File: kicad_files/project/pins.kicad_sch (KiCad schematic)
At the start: 0 parts

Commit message: started with board layout, also added more stuff on the schematic
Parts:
- added J3: Conn_02x11_Odd_Even, Connector_PinHeader_2.54mm:PinHeader_2x11_P2.54mm_Vertical, symbol Connector_Generic:Conn_02x11_Odd_Even
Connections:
- new net mprj_io.14: J3.1 (Pin_1)
- new net mprj_io.15: J3.2 (Pin_2)
- new net mprj_io.16: J3.3 (Pin_3)
- new net mprj_io.17: J3.4 (Pin_4)
- new net mprj_io.18: J3.5 (Pin_5)
- new net mprj_io.19: J3.6 (Pin_6)
- new net mprj_io.20: J3.7 (Pin_7)
- new net mprj_io.21: J3.8 (Pin_8)
- new net mprj_io.22: J3.9 (Pin_9)
- new net mprj_io.23: J3.10 (Pin_10)
- new net mprj_io.24: J3.11 (Pin_11)
- new net mprj_io.25: J3.12 (Pin_12)
- new net mprj_io.26: J3.13 (Pin_13)
- new net mprj_io.27: J3.14 (Pin_14)
- new net mprj_io.28: J3.15 (Pin_15)
- new net mprj_io.29: J3.16 (Pin_16)
- new net mprj_io.30: J3.17 (Pin_17)
- new net mprj_io.31: J3.18 (Pin_18)
- new net mprj_io.32: J3.19 (Pin_19)
- new net mprj_io.33: J3.20 (Pin_20)
- new net mprj_io.34: J3.21 (Pin_21)
- new net mprj_io.35: J3.22 (Pin_22)

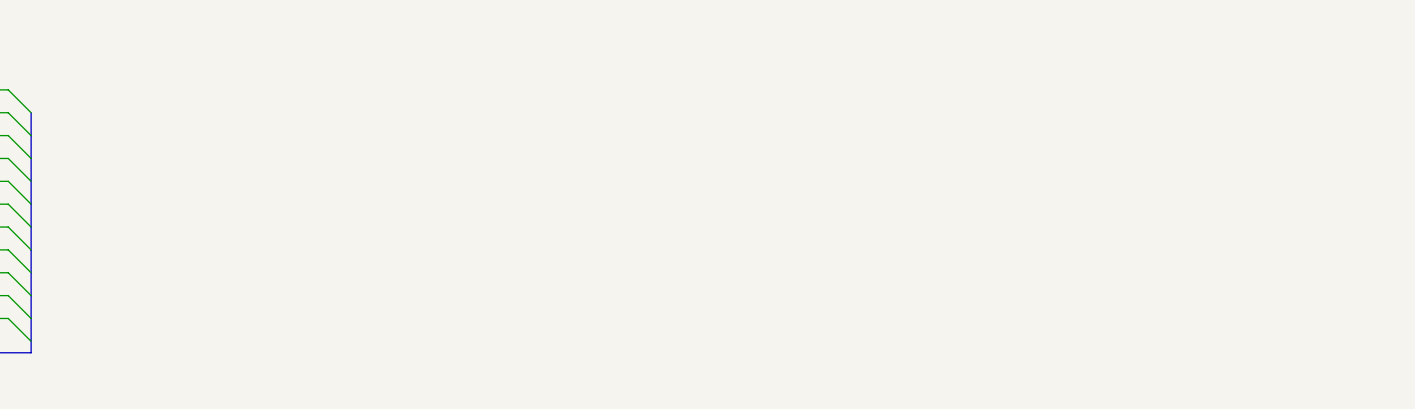
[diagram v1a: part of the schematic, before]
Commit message: clocking IC to the schematic with all needed connections, clocks still have to be connected
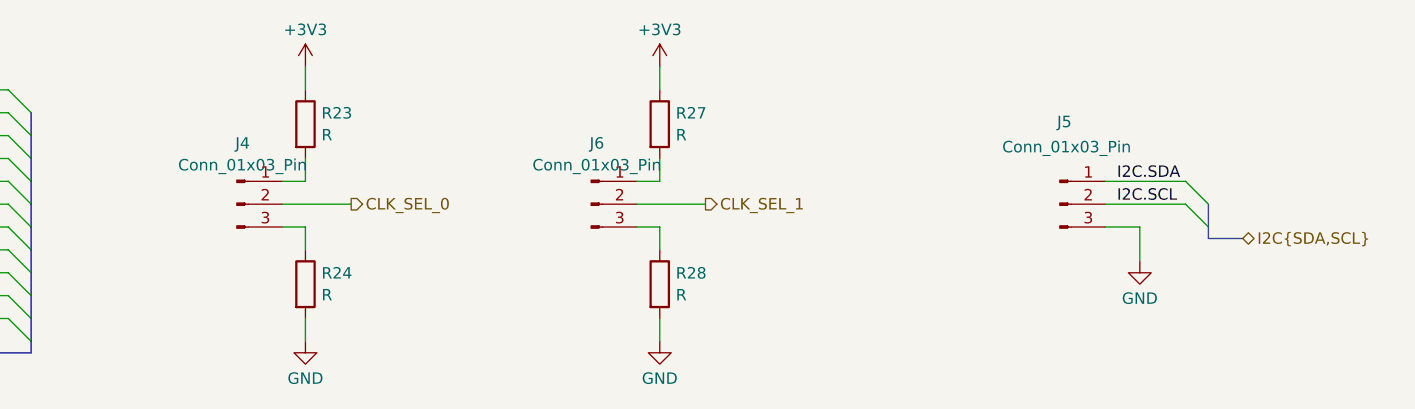
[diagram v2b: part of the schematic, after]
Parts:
- added J4, J5, J6: Conn_01x03_Pin, Connector_PinHeader_2.54mm:PinHeader_1x03_P2.54mm_Vertical, symbol Connector:Conn_01x03_Pin
- added R23, R24, R27, R28: R, Resistor_SMD:R_0805_2012Metric, symbol Device:R
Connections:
- new net: J6.1 (Pin_1), R27.2
- new net: J4.1 (Pin_1), R23.2
- new net: J4.3 (Pin_3), R24.1
- new net: J6.3 (Pin_3), R28.1
- new net +3V3: R23.1, R27.1
- new net CLK_SEL_0: J4.2 (Pin_2)
- new net CLK_SEL_1: J6.2 (Pin_2)
- new net GND: J5.3 (Pin_3), R24.2, R28.2
- new net I2C.SCL: J5.2 (Pin_2)
- new net I2C.SDA: J5.1 (Pin_1)

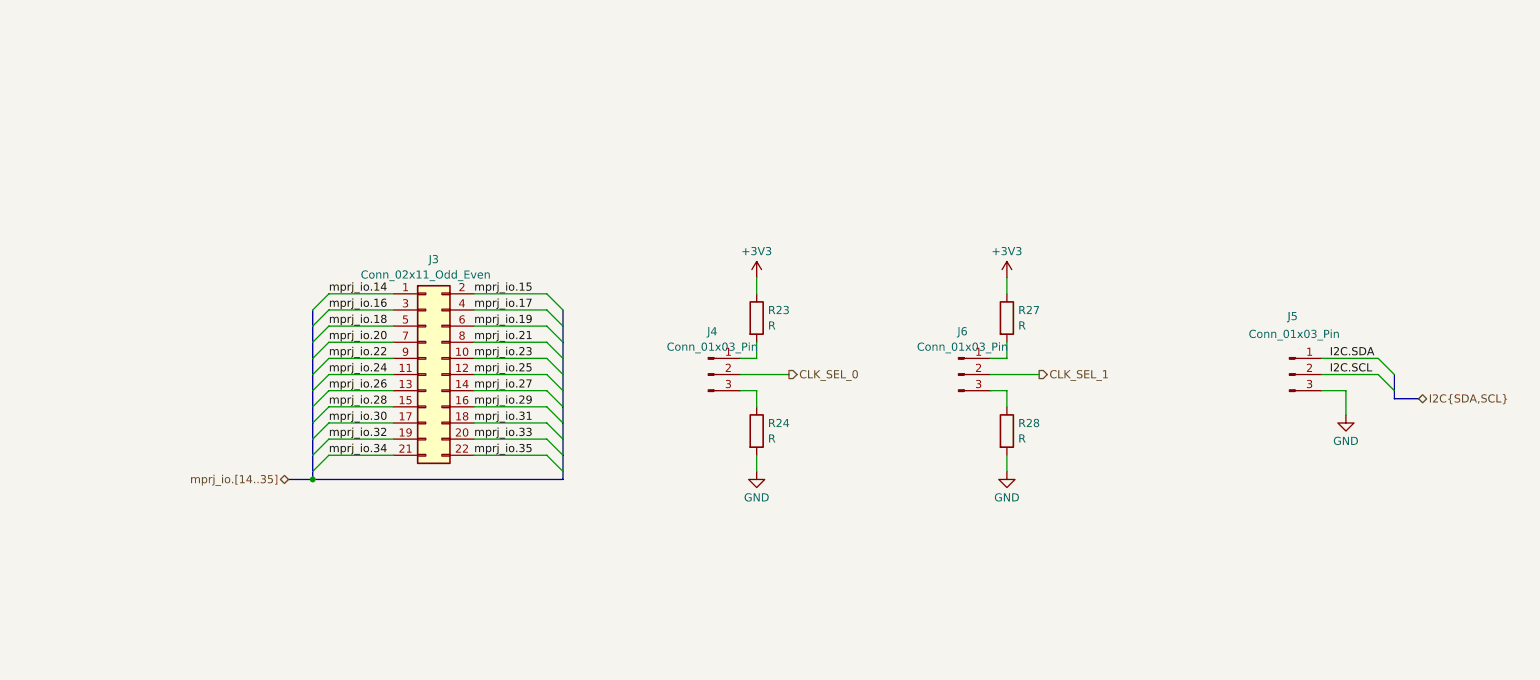
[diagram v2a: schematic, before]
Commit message: new layout, add more pin header, change the caravel power pin supply
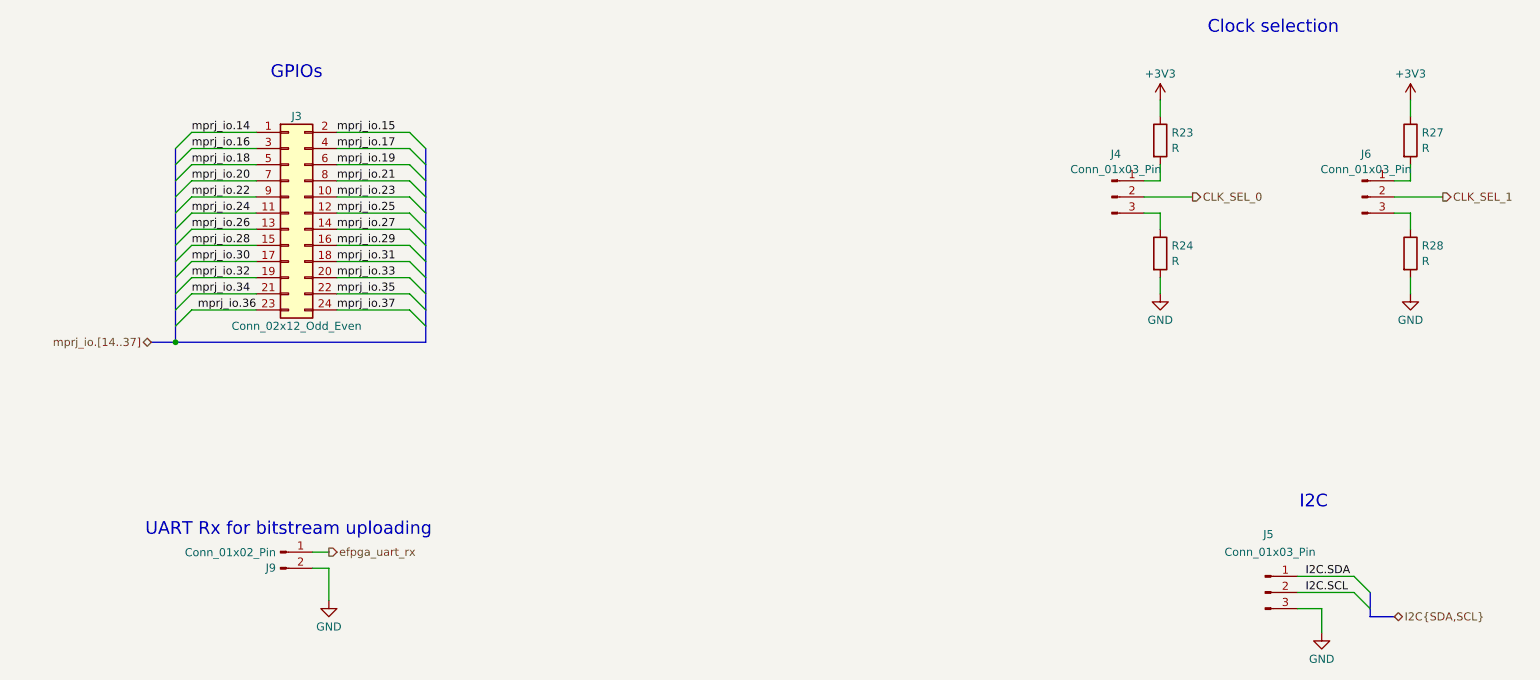
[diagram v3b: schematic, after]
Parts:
- added J9: Conn_01x02_Pin, Connector_PinHeader_2.54mm:PinHeader_1x02_P2.54mm_Vertical, symbol Connector:Conn_01x02_Pin
- J3: value Conn_02x11_Odd_Even -> Conn_02x12_Odd_Even; footprint Connector_PinHeader_2.54mm:PinHeader_2x11_P2.54mm_Vertical -> Connector_PinHeader_2.54mm:PinHeader_2x12_P2.54mm_Vertical; symbol Connector_Generic:Conn_02x11_Odd_Even -> Connector_Generic:Conn_02x12_Odd_Even
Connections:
- net GND: now also J9.2 (Pin_2)
- new net efpga_uart_rx: J9.1 (Pin_1)
- new net mprj_io.36: J3.23 (Pin_23)
- new net mprj_io.37: J3.24 (Pin_24)
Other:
- note added: "Clock selection"
- note added: "GPIOs"
- note added: "I2C"
- note added: "UART Rx for bitstream uploading"
- moved on the sheet: J4, J5, J6, R23, R24, R27, R28

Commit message: misc: simplifiy power pins and other components, add test pins
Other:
- title: (none) -> Pin Headers
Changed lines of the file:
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@@
 	(paper "A4")
 	(title_block
+		(title "Pin Headers")
 		(date "2024-05-30")
 		(rev "0.1")
